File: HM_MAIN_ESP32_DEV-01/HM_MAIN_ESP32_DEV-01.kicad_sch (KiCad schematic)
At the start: 3 parts, among them J2 Conn_02x19_Odd_Even, M1 ESP32-DEVKITV1

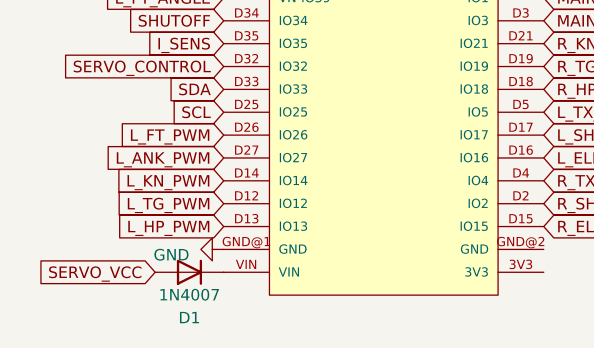
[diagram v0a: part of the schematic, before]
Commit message: arrumado código de teste do MPU e modelo dos diodos adicionado
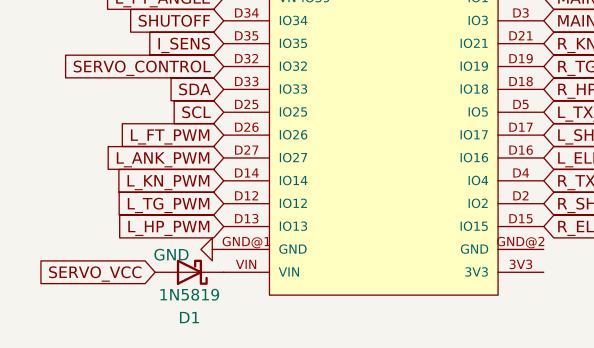
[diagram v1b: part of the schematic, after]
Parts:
- removed D1: 1N4007, Diode_THT:D_DO-41_SOD81_P10.16mm_Horizontal, symbol Diode:1N4007
- added D1: 1N5819, Diode_THT:D_A-405_P10.16mm_Horizontal, symbol Device:D_Schottky
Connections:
- net SERVO_VCC: now also D1.2 (A)
- net at M1.VIN: now also D1.1 (K)
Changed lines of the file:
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@@
     (pin "1")
     (instances
-      (project "HM_MAIN_ESP32-01"
+      (project "HM_MAIN_ESP32_DEV-01"
         (path "/a5d87afa-cb08-457a-8d0e-77c16130c40c"
           (reference "#PWR04") (unit 1)
-        )
-      )
-    )
-  )
-  (symbol (lib_id "Diode:1N4007") (at 41.91 116.84 180) (unit 1)
-    (in_bom yes) (on_board yes) (dnp no)
-    (property "Reference" "D1" (at 41.91 121.92 0)
-      (effects (font (size 1.27 1.27)))
-    )
-    (property "Value" "1N4007" (at 41.91 119.38 0)
-      (effects (font (size 1.27 1.27)))
-    )
-    (property "Footprint" "Diode_THT:D_DO-41_SOD81_P10.16mm_Horizontal" (at 41.91 112.395 0)
-      (effects (font (size 1.27 1.27)) hide)
-    )
-    (property "Datasheet" "http://www.vishay.com/docs/88503/1n4001.pdf" (at 41.91 116.84 0)
-      (effects (font (size 1.27 1.27)) hide)
-    )
-    (property "Sim.Device" "D" (at 41.91 116.84 0)
-      (effects (font (size 1.27 1.27)) hide)
-    )
-    (property "Sim.Pins" "1=K 2=A" (at 41.91 116.84 0)
-      (effects (font (size 1.27 1.27)) hide)
-    )
-    (pin "1")
-    (pin "2")
-    (instances
-      (project "HM_MAIN_ESP32-01"
-        (path "/a5d87afa-cb08-457a-8d0e-77c16130c40c"
-          (reference "D1") (unit 1)
         )
       )
@@
     (pin "1")
     (instances
-      (project "HM_MAIN_ESP32-01"
+      (project "HM_MAIN_ESP32_DEV-01"
         (path "/a5d87afa-cb08-457a-8d0e-77c16130c40c"
           (reference "#PWR0109") (unit 1)
@@
     (pin "VIN")
     (instances
-      (project "HM_MAIN_ESP32-01"
+      (project "HM_MAIN_ESP32_DEV-01"
         (path "/a5d87afa-cb08-457a-8d0e-77c16130c40c"
           (reference "M1") (unit 1)
@@
     (pin "1")
     (instances
-      (project "HM_MAIN_ESP32-01"
+      (project "HM_MAIN_ESP32_DEV-01"
         (path "/a5d87afa-cb08-457a-8d0e-77c16130c40c"
           (reference "#PWR01") (unit 1)
@@
     (pin "9")
     (instances
-      (project "HM_MAIN_ESP32-01"
+      (project "HM_MAIN_ESP32_DEV-01"
         (path "/a5d87afa-cb08-457a-8d0e-77c16130c40c"
           (reference "J2") (unit 1)
         )
       )
+    )
+  )
+  (symbol (lib_id "Device:D_Schottky") (at 41.91 116.84 180) (unit 1)
+    (in_bom yes) (on_board yes) (dnp no)
+    (property "Reference" "D1" (at 41.91 121.92 0)
+      (effects (font (size 1.27 1.27)))
+    )
+    (property "Value" "1N5819" (at 41.91 119.38 0)
+      (effects (font (size 1.27 1.27)))
+    )
+    (property "Footprint" "Diode_THT:D_A-405_P10.16mm_Horizontal" (at 41.91 116.84 0)
+      (effects (font (size 1.27 1.27)) hide)
+    )
+    (property "Datasheet" "~" (at 41.91 116.84 0)
+      (effects (font (size 1.27 1.27)) hide)
+    )
+    (pin "1")
+    (pin "2")
+    (instances
+      (project "HM_MAIN_ESP32_DEV-01"
+        (path "/a5d87afa-cb08-457a-8d0e-77c16130c40c"
+          (reference "D1") (unit 1)
+        )
+      )
